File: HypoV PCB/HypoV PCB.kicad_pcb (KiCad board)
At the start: 2 copper layers, 59 x 24 mm, 7 parts

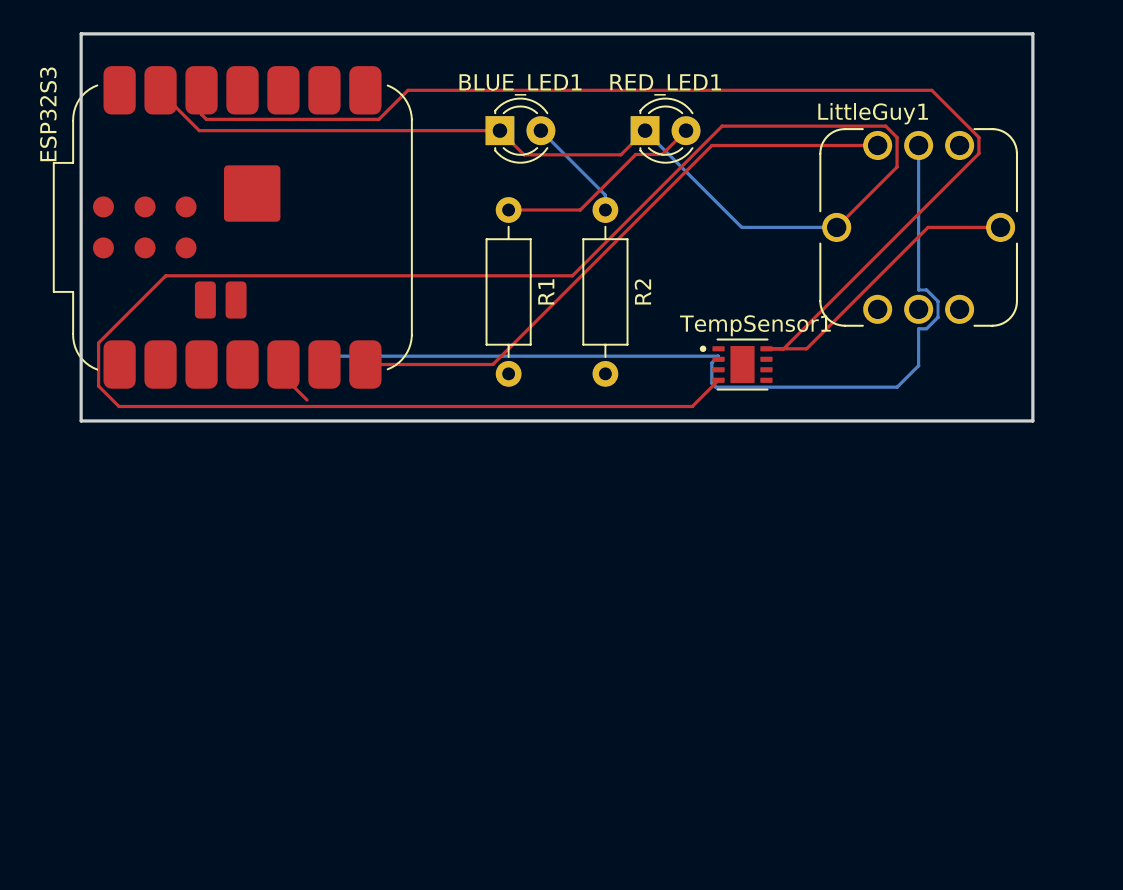
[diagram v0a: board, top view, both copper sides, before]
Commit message: started wiring up temp sensor according to datasheet
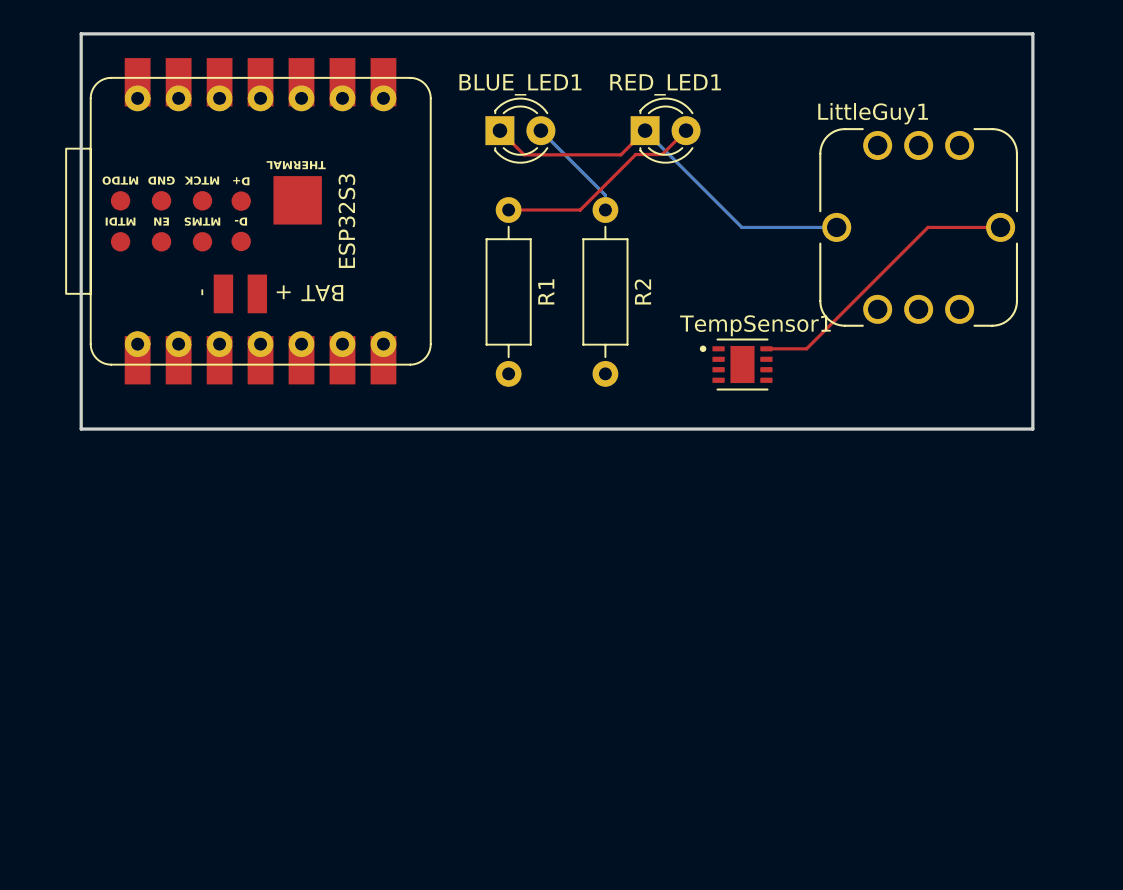
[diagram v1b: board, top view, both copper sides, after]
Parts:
- ESP32S3: footprint RF_Module:MCU_Seeed_ESP32C3 -> fab:SeeedStudio_XIAO_ESP32S3
- moved ESP32S3 1.18 mm to (81.1, 76.6)
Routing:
- net GND: track 151.5 -> 24.6 mm
- net +3.3V: track 88.6 -> 17.6 mm
- net /SCL: track 55.4 -> 0.00 mm
- net Net-(ESP32S3-TX_D6): track 37.4 -> 0.00 mm
- net /SDA: track 2.81 -> 0.00 mm
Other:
- board size 59 x 24 mm -> 59 x 24.5 mm

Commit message: more edits
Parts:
- added BYPASS_CAP_.1UF1: C_1206, PCM_fab:C_1206, F.Cu at (101.9, 92.6)
- added C1: C_1206, PCM_fab:C_1206, F.Cu at (101.9, 95.9)
- added J1: Conn_Header_JST_PH_1x02_P2mm_Vertical_SMD, PCM_fab:Header_JST_PH_1x02_P2mm_Vertical_SMD, B.Cu at (90.0, 76.9)
- added PULLUP_4.7K_R1: R_1206, PCM_fab:R_1206, F.Cu at (101.9, 99.1)
- added PULLUP_4.7K_R2: R_1206, PCM_fab:R_1206, F.Cu at (101.9, 102.4)
- added PULLUP_4.7K_R3: R_1206, PCM_fab:R_1206, F.Cu at (101.9, 105.6)
- ESP32S3: footprint fab:SeeedStudio_XIAO_ESP32S3 -> PCM_fab:SeeedStudio_XIAO_ESP32S3
- moved TempSensor1 11.4 mm to (119.5, 93.0)
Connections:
- ESP32S3 pad 15: (no net) -> GND
- ESP32S3 pad 16: (no net) -> Net-(ESP32S3-BAT_VIN)
- ESP32S3 pad 17: (no net) -> unconnected-(ESP32S3-MTDI-Pad17)
- ESP32S3 pad 18: (no net) -> unconnected-(ESP32S3-EN-Pad18)
- ESP32S3 pad 19: (no net) -> unconnected-(ESP32S3-MTMS-Pad19)
- ESP32S3 pad 2: Net-(ESP32S3-D1) -> unconnected-(ESP32S3-D1-Pad2)
- ESP32S3 pad 20: (no net) -> unconnected-(ESP32S3-MTCK-Pad20)
- ESP32S3 pad 21: (no net) -> unconnected-(ESP32S3-GND-Pad21)
- ESP32S3 pad 22: (no net) -> unconnected-(ESP32S3-MTDO-Pad22)
- ESP32S3 pad 23: (no net) -> unconnected-(ESP32S3-D--Pad23)
- ESP32S3 pad 24: (no net) -> unconnected-(ESP32S3-D+-Pad24)
- ESP32S3 pad 25: (no net) -> unconnected-(ESP32S3-THERMAL-Pad25)
- ESP32S3 pad 3: Net-(ESP32S3-D2) -> unconnected-(ESP32S3-D2-Pad3)
- ESP32S3 pad 7: Net-(ESP32S3-TX_D6) -> /OS
- LittleGuy1 pad INT: Net-(ESP32S3-TX_D6) -> unconnected-(LittleGuy1-PadINT)
- LittleGuy1 pad SCL: /SCL -> unconnected-(LittleGuy1-PadSCL)
- LittleGuy1 pad SCL1: unconnected-(LittleGuy1-SCL__1-PadSCL1) -> /SCL
- LittleGuy1 pad SDA: /SDA -> unconnected-(LittleGuy1-PadSDA)
- LittleGuy1 pad SDA1: unconnected-(LittleGuy1-SDA__1-PadSDA1) -> /SDA
- R1 pad 2: Net-(ESP32S3-D1) -> unconnected-(R1-Pad2)
- R2 pad 2: Net-(ESP32S3-D2) -> unconnected-(R2-Pad2)
- TempSensor1 pad 3: unconnected-(TempSensor1-OS-Pad3) -> /OS
- TempSensor1 pad 5: unconnected-(TempSensor1-A2-Pad5) -> GND
- TempSensor1 pad 6: unconnected-(TempSensor1-A1-Pad6) -> GND
- TempSensor1 pad 7: unconnected-(TempSensor1-A0-Pad7) -> GND
- TempSensor1 pad 9: unconnected-(TempSensor1-EPAD-Pad9) -> GND
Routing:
- net +3.3V: track 17.6 -> 0.00 mm
- net GND: track 24.6 -> 10.2 mm

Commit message: added final pcb stuff
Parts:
- removed the BYPASS_CAP_.1UF1 at (101.9, 92.6)
- BLUE_LED1, RED_LED1: moved to B.Cu
- R1, R2: footprint Resistor_THT:R_Axial_DIN0207_L6.3mm_D2.5mm_P10.16mm_Horizontal -> PCM_fab:R_1206
- moved BYPASS_CAP_.1UF1 25.6 mm to (126.5, 103.0), turned to -90 degrees
- moved J1 18.4 mm to (76.0, 88.9)
- moved RED_LED1 15.1 mm to (90.0, 73.2), turned to -90 degrees
- moved PULLUP_4.7K_R1 13.7 mm to (115.5, 100.5), turned to 180 degrees
- moved ESP32S3 13.3 mm to (81.1, 89.9)
- moved TempSensor1 12.0 mm to (120.5, 105.0)
- moved PULLUP_4.7K_R3 11.6 mm to (113.0, 109.0), turned to 90 degrees
- moved BLUE_LED1 9.31 mm to (105.0, 73.2), turned to -90 degrees
- moved PULLUP_4.7K_R2 6.79 mm to (108.5, 104.0), turned to 180 degrees
- moved R1 5.00 mm to (94.5, 80.5)
- moved R2 4.82 mm to (104.0, 80.5)
- turned LittleGuy1 to 90 degrees
- renumbered C1 to BYPASS_CAP_.1UF1
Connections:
- ESP32S3 pad 10: unconnected-(ESP32S3-D9-Pad10) -> /D9
- ESP32S3 pad 8: unconnected-(ESP32S3-D7-Pad8) -> Net-(ESP32S3-D7)
- ESP32S3 pad 9: unconnected-(ESP32S3-D8-Pad9) -> Net-(ESP32S3-D8)
- LittleGuy1 pad INT: unconnected-(LittleGuy1-PadINT) -> /D9
- LittleGuy1 pad SDA: unconnected-(LittleGuy1-PadSDA) -> /SDA
- R1 pad 2: unconnected-(R1-Pad2) -> Net-(ESP32S3-D7)
- R2 pad 2: unconnected-(R2-Pad2) -> Net-(ESP32S3-D8)
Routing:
- net +3.3V: track 0.00 -> 150.4 mm, vias 0 -> 3
- net /SDA: track 0.00 -> 81.5 mm
- net /SCL: track 0.00 -> 80.3 mm, vias 0 -> 1
- net GND: track 10.2 -> 73.9 mm, vias 0 -> 2
- net /D9: track 0.00 -> 38.2 mm
- net /OS: track 0.00 -> 35.3 mm
- net Net-(ESP32S3-D8): track 0.00 -> 20.4 mm
- net Net-(ESP32S3-BAT_VIN): track 0.00 -> 10.4 mm
- net Net-(ESP32S3-D7): track 0.00 -> 5.87 mm
- net Net-(RED_LED1-A): track 13.0 -> 7.60 mm
- net Net-(BLUE_LED1-A): track 6.58 -> 3.64 mm
- added copper zone on F.Cu, net GND
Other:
- board size 59 x 24.5 mm -> 61.5 x 43 mm

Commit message: CAD changes
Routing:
- net GND: track 73.9 -> 69.0 mm
- net Net-(ESP32S3-BAT_VIN): track 10.4 -> 11.9 mm
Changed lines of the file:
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@@
 			(outputformat 1)
 			(mirror no)
-			(drillshape 1)
+			(drillshape 0)
 			(scaleselection 1)
 			(outputdirectory "")
@@
 		(tags "resistor 1206")
 		(property "Reference" "PULLUP_4.7K_R3"
-			(at 0 -1.85 90)
+			(at -2 -8 0)
 			(layer "F.SilkS")
 			(effects
@@
 		)
 		(property "Value" "MAX30205MTA+T"
-			(at 9.755 2.362 0)
+			(at 5.015 5.975 0)
 			(layer "F.Fab")
 			(effects
@@
 		(tags "resistor 1206")
 		(property "Reference" "PULLUP_4.7K_R1"
-			(at 0 -1.85 0)
+			(at 8 -1.07 0)
 			(layer "F.SilkS")
 			(effects
@@
 		)
 		(fp_text user "${REFERENCE}"
-			(at 0 0 0)
+			(at 0 1.07 0)
 			(layer "F.Fab")
 			(effects
@@
 		)
 		(fp_text user "${REFERENCE}"
-			(at 0.0025 2.931 90)
+			(at 0.0025 10.551 90)
 			(unlocked yes)
 			(layer "F.Fab")
@@
 		(tags "capacitor 1206")
 		(property "Reference" "BYPASS_CAP_.1UF1"
-			(at 0.5 -2 90)
+			(at -3 -4.5 90)
 			(layer "F.SilkS")
 			(effects
@@
 		)
 		(fp_text user "${REFERENCE}"
-			(at 0 0 90)
+			(at 0.475 -1.07 90)
 			(layer "F.Fab")
 			(effects
@@
 		)
 		(property "Value" "Conn_Header_JST_PH_1x02_P2mm_Vertical_SMD"
-			(at 0 0.5 0)
+			(at -15.671 -0.9825 0)
 			(layer "B.Fab")
 			(effects
@@
 	)
 	(segment
-		(start 76 86.875)
-		(end 77.125 88)
+		(start 74 85.9)
+		(end 76 87.9)
 		(width 0.5)
 		(layer "B.Cu")
@@
 	)
 	(segment
-		(start 76 77)
-		(end 76 86)
+		(start 74 84.305)
+		(end 74 85.9)
 		(width 0.5)
 		(layer "B.Cu")
@@
 	)
 	(segment
-		(start 76 86)
-		(end 76 86.875)
+		(start 76.04 82.265)
+		(end 74 84.305)
 		(width 0.5)
 		(layer "B.Cu")
@@
 	)
 	(segment
-		(start 75.5 76.5)
-		(end 76 77)
-		(width 0.5)
-		(layer "B.Cu")
-		(net 1)
-	)
-	(segment
 		(start 100.5 104)
 		(end 107 104)
@@
 	)
 	(segment
-		(start 75 92.5)
-		(end 75 92.125)
+		(start 76 89.9)
+		(end 74.5 91.4)
 		(width 0.5)
 		(layer "B.Cu")
@@
 	)
 	(segment
-		(start 77 94.5)
-		(end 75 92.5)
-		(width 0.5)
-		(layer "B.Cu")
-		(net 14)
-	)
-	(segment
-		(start 75 92.125)
-		(end 77.125 90)
+		(start 74.5 94.5)
+		(end 81 94.5)
 		(width 0.5)
 		(layer "B.Cu")
@@
 	)
 	(segment
-		(start 81 94.5)
-		(end 77 94.5)
+		(start 74.5 91.4)
+		(end 74.5 94.5)
 		(width 0.5)
 		(layer "B.Cu")
@@
 		(hatch edge 0.5)
 		(connect_pads
-			(clearance 0.5)
+			(clearance 0.7)
 		)
-		(min_thickness 0.25)
+		(min_thickness 0.5)
 		(filled_areas_thickness no)
 		(fill yes
